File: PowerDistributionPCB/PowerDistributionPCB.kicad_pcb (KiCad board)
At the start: 4 copper layers, 92.3 x 122.5 mm, 86 parts, among them K1 RT314F05(gen), K2 RT314F05(gen), K3 RT314F05(gen), K4 RT314F05(gen), Q1 AOD4185, Q10 MMBT2222A, Q11 MMBT2222A, Q12 MMBT2222A, Q2 MMBT2222A, Q6 MMBT2222A, Q7 MMBT2222A, Q8 MMBT2222A, Q9 MMBT2222A, U1 AP63203WU

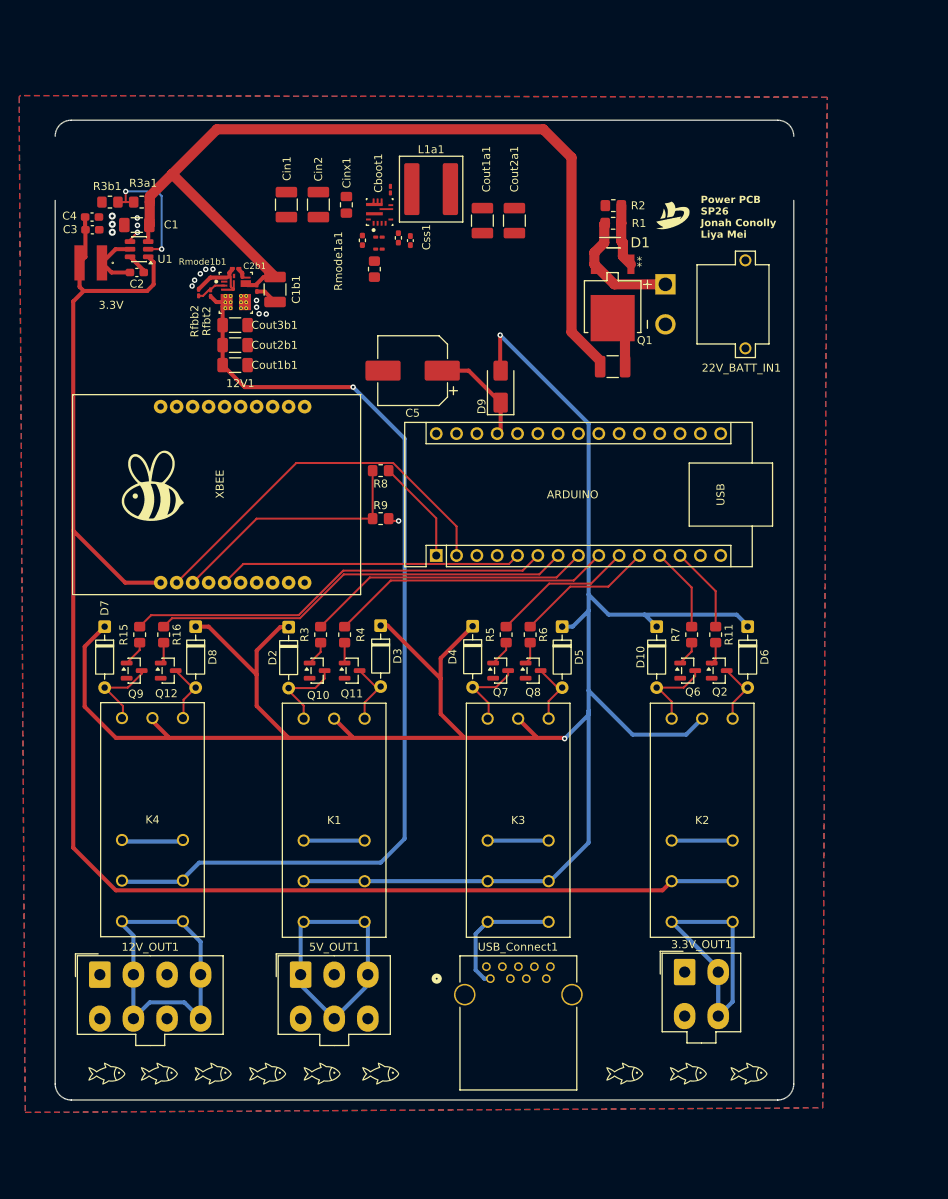
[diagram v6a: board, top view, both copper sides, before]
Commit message: new 5V buck basically done
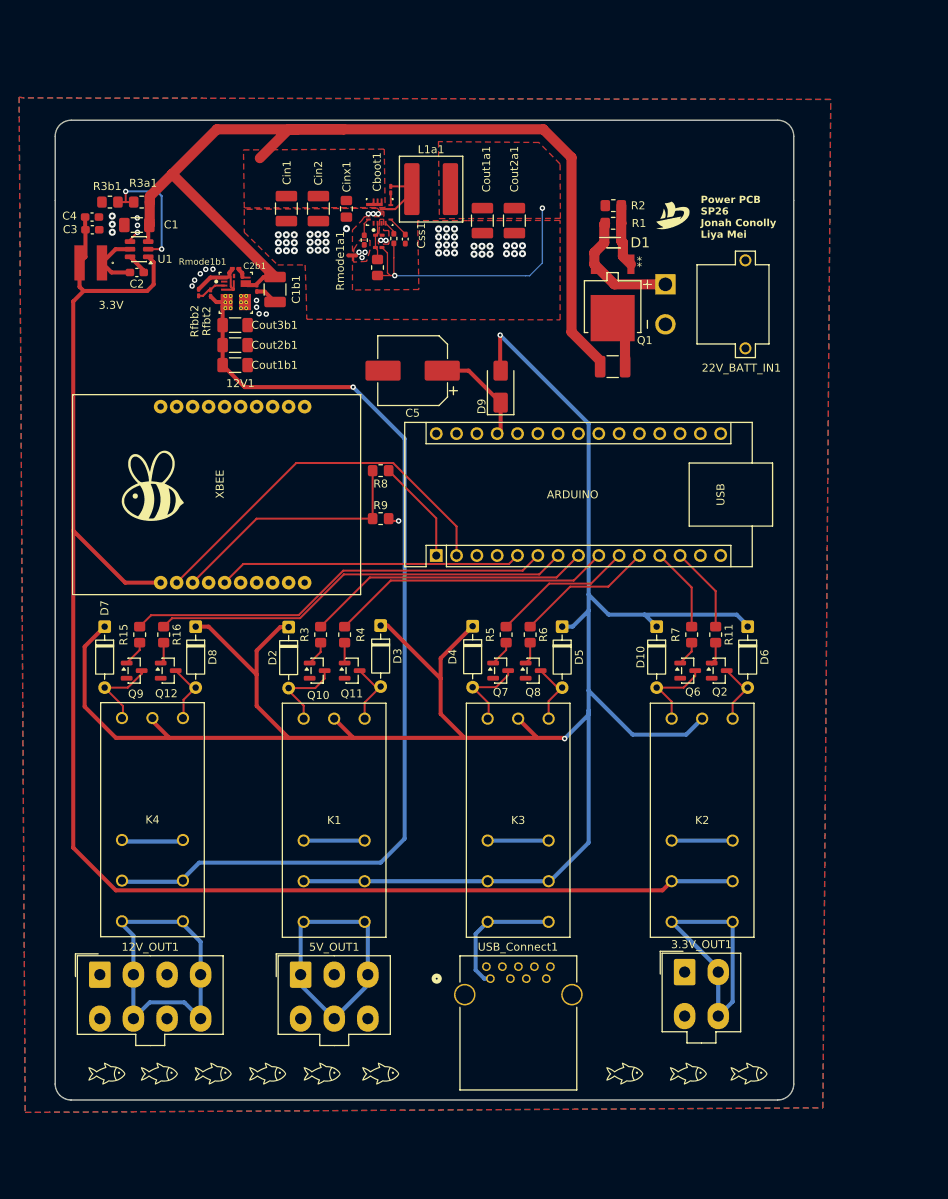
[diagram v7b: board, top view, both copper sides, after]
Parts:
- added NT1: NetTie_2, NetTie:NetTie-2_SMD_Pad0.5mm, F.Cu at (90.6, 53.3)
- 5V1: footprint CUSail:TPS56A37RPAR -> CUSail:RPA0010A-MFG
- moved Css1 0.67 mm to (97.3, 51.2)
- moved Rpg1 0.58 mm to (95.8, 51.2)
- moved Cin1 0.50 mm to (82.4, 47.4)
- moved Cin2 0.50 mm to (86.4, 47.4)
- moved Cinx1 0.50 mm to (89.9, 47.5)
- moved Rfbt1 0.44 mm to (93.8, 54.8)
- moved Rfbb1 0.24 mm to (94.0, 50.8)
- moved Rmode1a1 0.23 mm to (92.1, 51.4)
- moved Cff1 0.20 mm to (93.9, 52.3)
- turned Cboot1 to -90 degrees
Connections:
- 5V1 pad 3: GND -> GND1
- Css1 pad 2: GND -> GND1
- Rfbb1 pad 2: GND -> GND1
- Rmode1a1 pad 2: GND -> GND1
- Rpg1 pad 2: GND -> 5VBuck
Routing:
- net 5VBuck: track 297.9 -> 334.1 mm, vias 2 -> 4
- net Sys_Vin: track 112.0 -> 124.8 mm
- net Net-(5V1-SW): track 0.00 -> 7.24 mm
- net Net-(5V1-FB): track 0.00 -> 4.92 mm
- net Net-(5V1-SS): track 0.00 -> 2.62 mm
- net Net-(5V1-MODE): track 0.00 -> 2.19 mm
- net Net-(5V1-PG): track 0.00 -> 1.74 mm
- net Net-(5V1-BOOT): track 0.00 -> 1.53 mm
- net GND1: vias 0 -> 5
- net GND: vias 7 -> 53
- added copper zone on F.Cu, net 5VBuck
- added copper zone on F.Cu, net GND1
- added copper zone on In1.Cu, net GND1
- added copper zone on F.Cu, net Sys_Vin

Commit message: finished final updates
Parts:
- added G***: LOGO, LOGO, F.Cu at (126.5, 84.1)
- added G***: LOGO, LOGO, F.Cu at (106.2, 81.3)
- added H1: MountingHole, MountingHole:MountingHole_3.2mm_M3, F.Cu at (55.6, 36.9)
- added H2: MountingHole, MountingHole:MountingHole_3.2mm_M3, F.Cu at (144.5, 36.9)
- added H3: MountingHole, MountingHole:MountingHole_3.2mm_M3, F.Cu at (55.3, 155.9)
- added H4: MountingHole, MountingHole:MountingHole_3.2mm_M3, F.Cu at (144.6, 155.4)
- moved Main_Bulk 27.1 mm to (125.0, 40.1)
- moved R2 13.3 mm to (124.9, 60.3), turned to 180 degrees
- moved Q1 12.2 mm to (125.0, 47.6), turned to 0 degrees
- moved R1 8.93 mm to (124.9, 58.0), turned to 180 degrees
- moved G*** 5.17 mm to (133.1, 43.7)
- moved D1 4.24 mm to (124.9, 55.6), turned to 180 degrees
- moved 22V_BATT_IN 2.80 mm to (141.2, 57.0)
- moved G*** 2.15 mm to (68.7, 155.5)
- moved G*** 2.15 mm to (89.0, 155.5)
- moved G*** 2.15 mm to (82.2, 155.5)
- moved G*** 2.15 mm to (62.1, 155.5)
- moved G*** 2.15 mm to (75.4, 155.5)
- moved G*** 2.15 mm to (96.3, 155.5)
- moved G*** 1.67 mm to (138.6, 155.6)
- moved Cinx1 1.10 mm to (91.0, 47.2)
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- renumbered 12V1 to 12V, 22V_BATT_IN1 to 22V_BATT_IN, Main_Bulk(electrolytic)1 to Main_Bulk
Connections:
- 12V_OUT1 pad 1: GND -> 12VRelayOut
- 12V_OUT1 pad 3: GND -> 12VRelayOut
- 12V_OUT1 pad 6: 12VRelayOut -> GND
- 12V_OUT1 pad 8: 12VRelayOut -> GND
- 3.3V_OUT1 pad 1: GND -> 3.3VRelayOut
- 3.3V_OUT1 pad 4: 3.3VRelayOut -> GND
- 5V_OUT1 pad 2: GND -> 5VRelayOut
- 5V_OUT1 pad 5: 5VRelayOut -> GND
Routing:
- net 3.3VBuck: track 191.5 -> 35.6 mm, vias 0 -> 2
- net Sys_Vin: track 124.8 -> 3.86 mm, vias 0 -> 13
- net 12VBuck: track 125.0 -> 12.9 mm, vias 1 -> 2
- net 5VBuck: track 334.1 -> 272.5 mm, vias 4 -> 17
- net 12VRelayOut: track 43.7 -> 0.00 mm
- net 3.3VRelayOut: track 34.3 -> 0.46 mm
- net 5VRelayOut: track 35.6 -> 3.70 mm
- net Batt_Vin: track 15.6 -> 0.16 mm
- net Net-(U1-SW): track 8.22 -> 0.00 mm
- net GND: track 29.2 -> 37.3 mm, vias 53 -> 134
- net Net-(D1-A): track 7.84 -> 0.03 mm
- net Net-(Q1-D): track 6.84 -> 3.08 mm
- net Net-(5V1-SW): track 7.24 -> 3.62 mm
- net VNRelayOut: track 17.1 -> 16.6 mm
- net Net-(D8-A): track 8.04 -> 7.53 mm
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- added copper zone on F.Cu, net 12VBuck
- added copper zone on In2.Cu, net 12VBuck
- added copper zone on B.Cu, net 12VRelayOut
- added copper zone on F.Cu, net 12VRelayOut
- added copper zone on In2.Cu, net 12VRelayOut
- added copper zone on B.Cu, net 3.3VBuck
- added copper zone on F.Cu, net 3.3VBuck
- added copper zone on In2.Cu, net 3.3VBuck
- added copper zone on B.Cu, net 3.3VRelayOut
- added copper zone on F.Cu, net 3.3VRelayOut
- added copper zone on In2.Cu, net 3.3VRelayOut
- added copper zone on B.Cu, net 5VBuck
- added copper zone on In2.Cu, net 5VBuck
- added copper zone on B.Cu, net 5VRelayOut
- added copper zone on F.Cu, net 5VRelayOut
- added copper zone on In2.Cu, net 5VRelayOut
- added copper zone on F.Cu, net Batt_Vin
- added copper zone on F.Cu, net Net-(5V1-SW)
- added copper zone on F.Cu, net Net-(D1-A)
- added copper zone on F.Cu, net Net-(Q1-D)
- added copper zone on F.Cu, net Net-(U1-SW)
- added copper zone on B.Cu, net Sys_Vin
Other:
- board size 92.3 x 122.5 mm -> 96 x 125.6 mm
- board text added: "5V"
